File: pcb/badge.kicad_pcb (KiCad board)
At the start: 2 copper layers, 35 x 22 mm, 26 parts, among them IC102 AAT3681A, P1 CONN_01X04, P102 CONN_01X02, P103 USB_OTG, P2 CONNECTOR, P3 CONNECTOR, Q1 NPN, Q101 FT230XS-R, Q102 NPN

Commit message: first complete version
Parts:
- removed 0R1, 0R2, 0R3, R1, R107, R108, R2, R3, R4, R5: R, netl:SMD_0603
- removed C1: 10u, netl:SMD_0603
- removed D1, D2, D3: LED, netl:SMD_0603
- removed P1: CONN_01X04, Pin_Headers:Pin_Header_Angled_1x04
- removed P2, P3: CONNECTOR, netl:1Pin_small
- removed Q1: NPN, TO_SOT_Packages_SMD:SOT-323
- removed R6: 0R, netl:SMD_0603
- added 0R101: R, netl:SMD_0603, F.Cu at (137.5, 72.5)
- added 0R102: R, netl:SMD_0603, F.Cu at (142.5, 72.5)
- added 0R103: R, netl:SMD_0603, F.Cu at (140.0, 72.5)
- added C101: 10u, netl:SMD_0603, F.Cu at (139.0, 85.0)
- added C102: 10u, netl:SMD_0603, F.Cu at (133.1, 79.4)
- added C103: C, netl:SMD_0603, F.Cu at (125.0, 88.0)
- added D101: LED, netl:SMD_0603, F.Cu at (124.0, 75.5)
- added G***: LOGO, netl:LOGO_127mm_Bottom_SS, F.Cu at (132.5, 80.0)
- added IC101: CH340G, Housings_SOIC:SOIC-16_3.9x9.9mm_Pitch1.27mm, F.Cu at (132.5, 85.0)
- added P101: CONN_01X02, Pin_Headers:Pin_Header_Straight_1x02, F.Cu at (120.1, 72.5)
- added R101: R, netl:SMD_0603, F.Cu at (124.0, 77.0)
- added R102: R, netl:SMD_0603, F.Cu at (141.5, 81.5)
- added R103: R, netl:SMD_0603, F.Cu at (144.0, 83.0)
- added R104: R, netl:SMD_0603, F.Cu at (135.5, 75.0)
- added R106: R, netl:SMD_0603, F.Cu at (144.0, 79.0)
- added REF**: via, netl:via, F.Cu at (129.1, 73.5)
- added REF**: via, netl:via, F.Cu at (130.2, 85.2)
- added REF**: via, netl:via, F.Cu at (146.2, 80.8)
- added REF**: via, netl:via, F.Cu at (142.3, 75.1)
- added REF**: via, netl:via, F.Cu at (137.2, 75.1)
- added REF**: via, netl:via, F.Cu at (139.6, 78.0)
- added REF**: via, netl:via, F.Cu at (138.5, 82.1)
- added REF**: via, netl:via, F.Cu at (130.8, 76.8)
- added x101: xtal_osc, netl:SM_3225, F.Cu at (125.0, 85.0)
- C104: value 10u -> C
- IC102: value AAT3681A -> TP4056; footprint netl:SC70JW-8 -> SMD_Packages:SOIC-8-N
- P102: value CONN_01X02 -> USB_OTG; footprint Pin_Headers:Pin_Header_Straight_1x02 -> Connect:USB_Micro-B
- P103: value USB_OTG -> CONN_01X05; footprint Connect:USB_Micro-B -> Pin_Headers:Pin_Header_Angled_1x05
- Q101: value FT230XS-R -> NPN; footprint Housings_SSOP:SSOP-16_5.3x6.2mm_Pitch0.65mm -> TO_SOT_Packages_SMD:SOT-323
- moved IC102 51.1 mm to (130.0, 75.0), turned to 90 degrees
- moved P103 50.9 mm to (147.5, 74.5), turned to 0 degrees
- moved R105 48.0 mm to (141.5, 78.0), turned to 90 degrees
- moved P102 46.3 mm to (117.5, 80.0), turned to 270 degrees
- moved C104 46.2 mm to (125.0, 82.0)
- moved Q102 39.1 mm to (144.0, 77.0)
- moved Q101 38.2 mm to (144.0, 81.0), turned to 90 degrees
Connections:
- C104 pad 1: V_USB -> Net-(C104-Pad1)
- IC102 pad 1: V_USB -> (no net)
- IC102 pad 3: VBat -> GND
- IC102 pad 5: chrg -> VBat
- IC102 pad 6: GND -> (no net)
- IC102 pad 7: GND -> Net-(D101-Pad1)
- IC102 pad 8: GND -> V_USB
- P102 pad 1: VBat -> V_USB
- P102 pad 2: GND -> D-
- P103 pad 1: V_USB -> VBat
- P103 pad 2: Net-(P103-Pad2) -> AVR_TX
- P103 pad 3: D+ -> AVR_RX
- P103 pad 4: Net-(P103-Pad4) -> AVR_VCC
- Q101 pad 2: Net-(P2-Pad1) -> TX
- Q101 pad 3: 3V3 -> AVR_RX
- Q102 pad 3: Net-(Q101-Pad4) -> RX
- R105 pad 1: Net-(IC102-Pad2) -> 3V3
- R105 pad 2: GND -> RX
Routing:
- net GND: track 42.0 -> 0.16 mm
- net 3V3: track 57.9 -> 24.4 mm, vias 2 -> 3
- net VBat: track 21.9 -> 50.4 mm, vias 0 -> 2
- net Net-(Q101-Pad1): track 18.1 -> 1.61 mm
- net Net-(Q101-Pad4): track 14.1 -> 0.00 mm
- net RX: track 0.00 -> 12.4 mm
- net Net-(C104-Pad1): track 0.00 -> 9.55 mm
- net TX: track 0.00 -> 9.46 mm
- net Net-(C103-Pad1): track 0.00 -> 7.94 mm
- net Net-(D3-Pad1): track 7.31 -> 0.00 mm
- net Net-(D2-Pad1): track 5.87 -> 0.00 mm
- net AVR_VCC: track 18.5 -> 24.1 mm, vias 0 -> 2
- net D-: track 9.24 -> 13.8 mm
- net AVR_TX: track 7.09 -> 2.82 mm
- net chrg: track 4.10 -> 0.00 mm
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- added copper zone on B.Cu, net GND
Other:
- board size 35 x 22 mm -> 35 x 20 mm

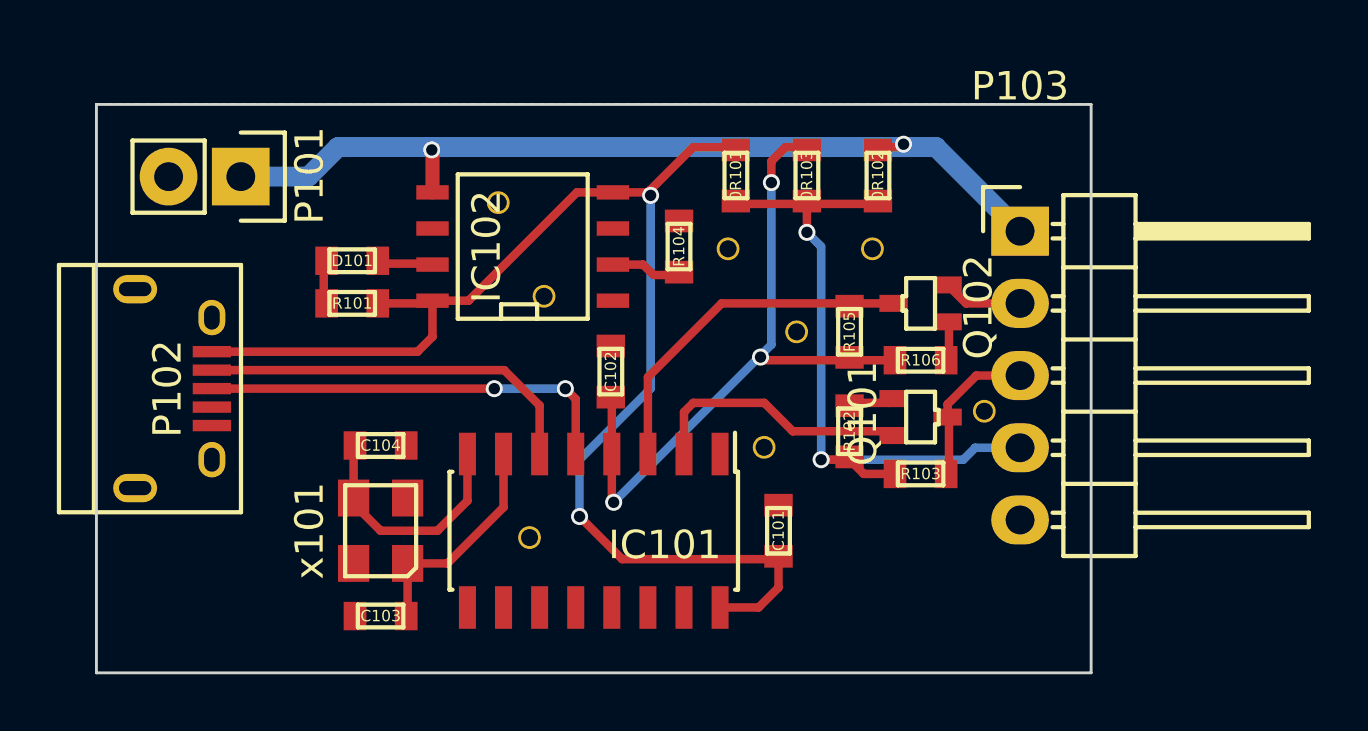
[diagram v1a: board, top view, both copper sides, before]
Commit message: updated layout to match schema
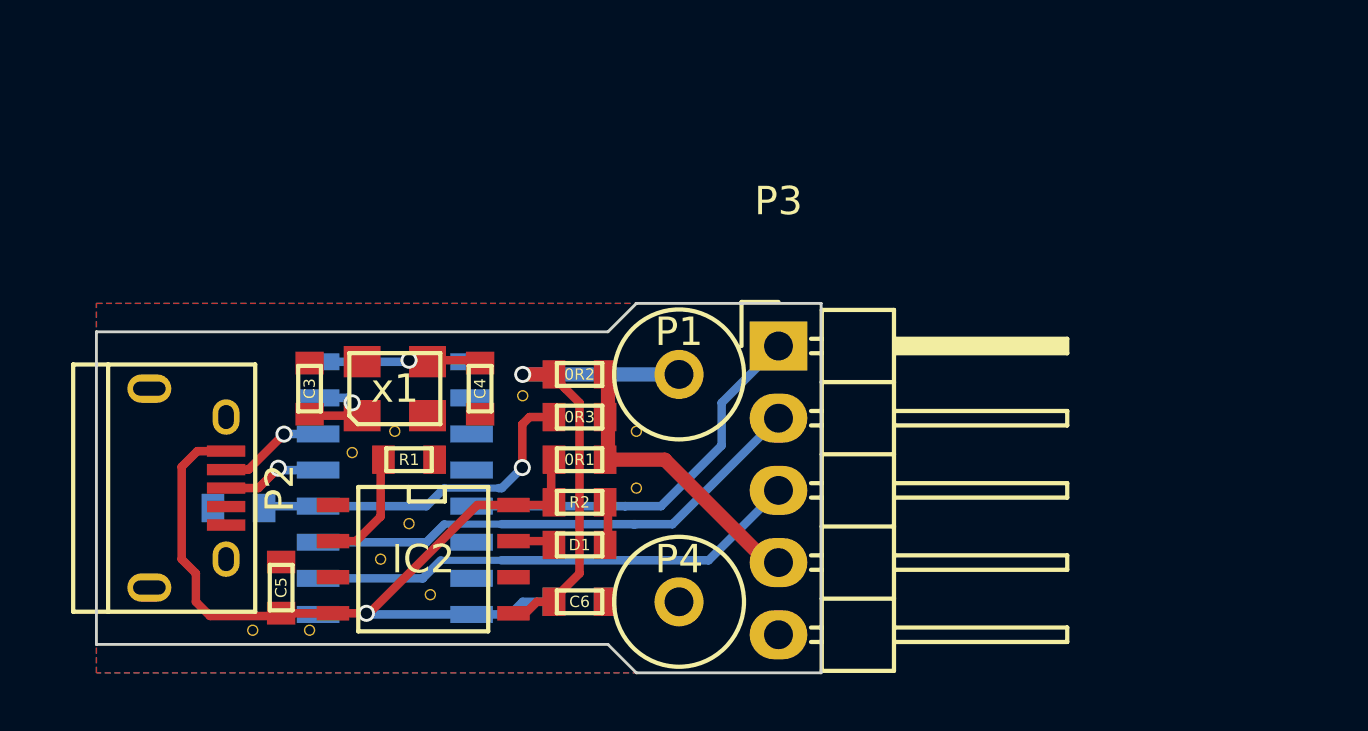
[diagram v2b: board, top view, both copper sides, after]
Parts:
- removed 0R101, 0R102, 0R103, R101, R102, R103, R104, R105, R106: R, netl:SMD_0603
- removed C101, C102: 10u, netl:SMD_0603
- removed C103, C104: C, netl:SMD_0603
- removed D101: LED, netl:SMD_0603
- removed G***: LOGO, netl:LOGO_127mm_Bottom_SS
- removed IC101: CH340G, Housings_SOIC:SOIC-16_3.9x9.9mm_Pitch1.27mm
- removed IC102: TP4056, SMD_Packages:SOIC-8-N
- removed P101: CONN_01X02, Pin_Headers:Pin_Header_Straight_1x02
- removed P102: USB_OTG, Connect:USB_Micro-B
- removed P103: CONN_01X05, Pin_Headers:Pin_Header_Angled_1x05
- removed Q101, Q102: NPN, TO_SOT_Packages_SMD:SOT-323
- removed the REF** at (129.1, 73.5)
- removed the REF** at (130.2, 85.2)
- removed the REF** at (146.2, 80.8)
- removed the REF** at (142.3, 75.1)
- removed the REF** at (137.2, 75.1)
- removed the REF** at (139.6, 78.0)
- removed the REF** at (138.5, 82.1)
- removed the REF** at (130.8, 76.8)
- removed x101: xtal_osc, netl:SM_3225
- added 0R1: R, netl:SMD_0603, F.Cu at (132.0, 82.5)
- added 0R2: R, netl:SMD_0603, F.Cu at (132.0, 79.5)
- added 0R3: R, netl:SMD_0603, F.Cu at (132.0, 81.0)
- added C1: 10u, netl:SMD_0603, B.Cu at (132.0, 87.5)
- added C2: 10u, netl:SMD_0603, B.Cu at (120.0, 84.2)
- added C3: 22p, netl:SMD_0603, F.Cu at (122.5, 80.0)
- added C4: 22p, netl:SMD_0603, F.Cu at (128.5, 80.0)
- added C5: 10u, netl:SMD_0603, F.Cu at (121.5, 87.0)
- added C6: 10u, netl:SMD_0603, F.Cu at (132.0, 87.5)
- added D1: LED, netl:SMD_0603, F.Cu at (132.0, 85.5)
- added IC1: CH340G, Housings_SOIC:SOIC-16_3.9x9.9mm_Pitch1.27mm, B.Cu at (125.5, 83.5)
- added IC2: TP4056, SMD_Packages:SOIC-8-N, F.Cu at (126.5, 86.0)
- added P1: CONN_01X01, Connect:1pin, F.Cu at (135.5, 79.5)
- added P2: USB_OTG, Connect:USB_Micro-B, F.Cu at (118.0, 83.5)
- added P3: CONN_01X05, Pin_Headers:Pin_Header_Angled_1x05, F.Cu at (139.0, 78.5)
- added P4: CONN_01X01, Connect:1pin, F.Cu at (135.5, 87.5)
- added R1: 2k, netl:SMD_0603, F.Cu at (126.0, 82.5)
- added R2: 1k, netl:SMD_0603, F.Cu at (132.0, 84.0)
- added REF**: via, netl:via, F.Cu at (130.0, 80.2)
- added REF**: via, netl:via, F.Cu at (134.0, 81.5)
- added REF**: via, netl:via, F.Cu at (120.5, 88.5)
- added REF**: via, netl:via, F.Cu at (122.5, 88.5)
- added REF**: via, netl:via, F.Cu at (126.8, 87.2)
- added REF**: via, netl:via, F.Cu at (126.0, 84.8)
- added REF**: via, netl:via, F.Cu at (125.0, 86.0)
- added REF**: via, netl:via, F.Cu at (124.0, 82.2)
- added REF**: via, netl:via, F.Cu at (125.5, 81.5)
- added REF**: via, netl:via, F.Cu at (134.0, 83.5)
- added x1: xtal_osc, netl:SM_3225, F.Cu at (125.5, 80.0)
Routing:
- net VBat: track 50.4 -> 16.8 mm, vias 2 -> 1
- net AVR_VCC: track 24.1 -> 0.00 mm, vias 2 -> 0
- net V_USB: track 47.8 -> 29.6 mm, vias 2 -> 1
- net ~DTR: track 0.00 -> 14.0 mm
- net 3V3: track 24.4 -> 12.2 mm, vias 3 -> 1
- net D+: track 14.9 -> 3.55 mm, vias 2 -> 1
- net U_OUT: track 0.00 -> 10.00 mm
- net D-: track 13.8 -> 3.76 mm, vias 0 -> 1
- net Net-(C104-Pad1): track 9.55 -> 0.00 mm
- net TX: track 9.46 -> 17.5 mm
- net Net-(C103-Pad1): track 7.94 -> 0.00 mm
- net Net-(C4-Pad1): track 0.00 -> 5.76 mm, vias 0 -> 1
- net RX: track 12.4 -> 18.2 mm
- net AVR_RX: track 5.44 -> 0.00 mm
- net Net-(IC2-Pad2): track 0.00 -> 4.03 mm
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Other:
- board size 35 x 20 mm -> 25.5 x 13 mm

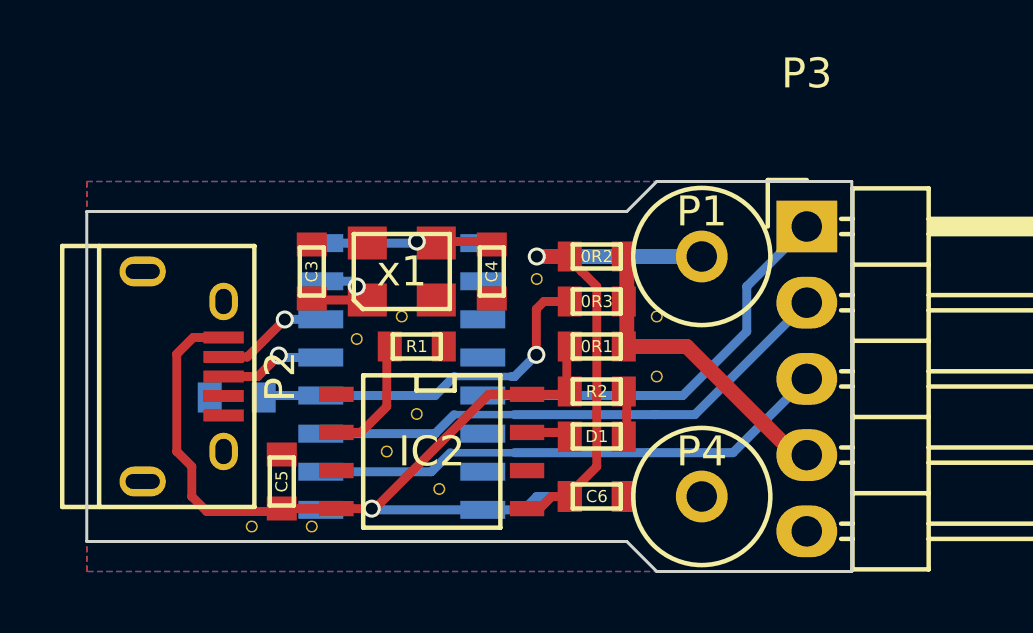
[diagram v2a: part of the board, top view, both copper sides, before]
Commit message: removed 3V3 selection. cleaned up layout
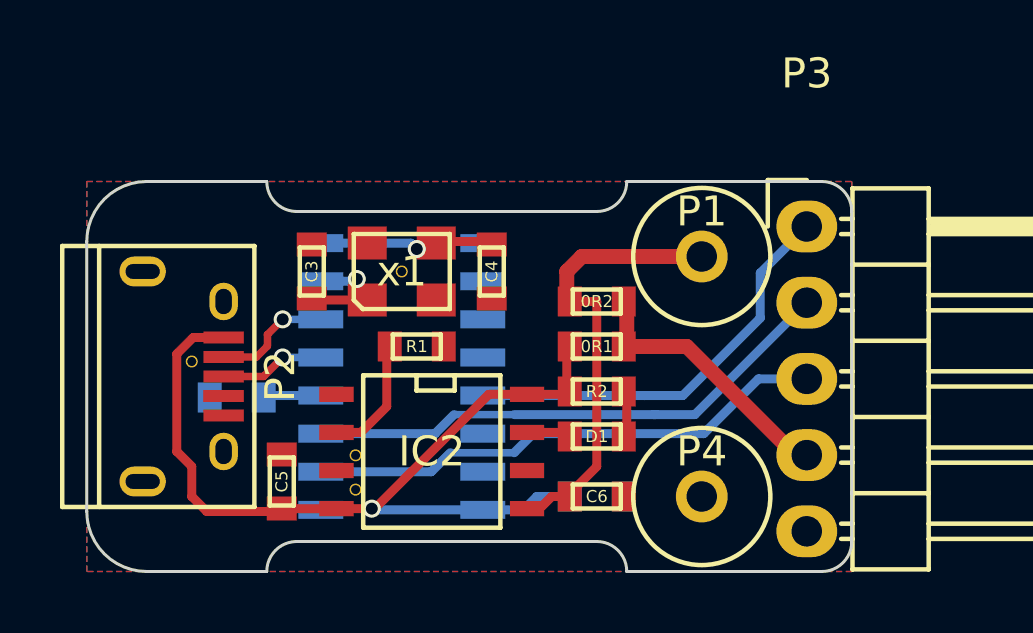
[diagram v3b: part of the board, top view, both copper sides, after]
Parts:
- removed 0R3: R, netl:SMD_0603
- removed the REF** at (130.0, 80.2)
- removed the REF** at (134.0, 81.5)
- removed the REF** at (120.5, 88.5)
- removed the REF** at (122.5, 88.5)
- removed the REF** at (126.8, 87.2)
- removed the REF** at (126.0, 84.8)
- removed the REF** at (125.0, 86.0)
- removed the REF** at (124.0, 82.2)
- removed the REF** at (125.5, 81.5)
- removed the REF** at (134.0, 83.5)
- added REF**: via, netl:via, F.Cu at (118.5, 83.0)
- added REF**: via, netl:via, F.Cu at (125.5, 80.0)
- added REF**: via, netl:via, F.Cu at (124.0, 87.3)
- added REF**: via, netl:via, F.Cu at (124.0, 86.1)
- 0R1, 0R2: value R -> 0R
- moved 0R2 1.50 mm to (132.0, 81.0)
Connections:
- IC1 pad 10: (no net) -> Net-(IC1-Pad10)
- IC1 pad 11: (no net) -> Net-(IC1-Pad11)
- IC1 pad 12: (no net) -> Net-(IC1-Pad12)
- IC1 pad 14: (no net) -> Net-(IC1-Pad14)
- IC1 pad 15: (no net) -> Net-(IC1-Pad15)
- IC1 pad 9: (no net) -> Net-(IC1-Pad9)
- IC2 pad 1: (no net) -> Net-(IC2-Pad1)
- IC2 pad 6: (no net) -> Net-(IC2-Pad6)
- P2 pad 4: (no net) -> Net-(P2-Pad4)
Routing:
- net 3V3: track 12.2 -> 1.83 mm, vias 1 -> 0
- net VBat: track 16.8 -> 15.1 mm, vias 1 -> 0
- net U_OUT: track 10.00 -> 8.50 mm
- net GND: track 0.00 -> 0.54 mm
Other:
- outline, holes or cut-outs redrawn
- net class Default: clearance 0.2 -> 0.1524
- rule trace_clearance: 0.2 -> 0.1524
